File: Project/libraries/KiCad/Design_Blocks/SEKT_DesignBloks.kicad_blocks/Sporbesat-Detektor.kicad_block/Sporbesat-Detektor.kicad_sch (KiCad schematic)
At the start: 14 parts, among them J1 Screw_Terminal_01x02, J2 Screw_Terminal_01x02, J4 Conn_01x05_Socket, Q1 BC857, U1 PC847

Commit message: DCC signal
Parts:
- added R3: 2.2kΩ, PCM_JLCPCB:R_0805, symbol PCM_JLCPCB-Resistors:0805,1.8kΩ
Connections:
- net GNDDCC: now also R3.1
- net at C1.1, Q1.3 (C), R2.1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: now also R3.2
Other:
- moved on the sheet: C1, TP2

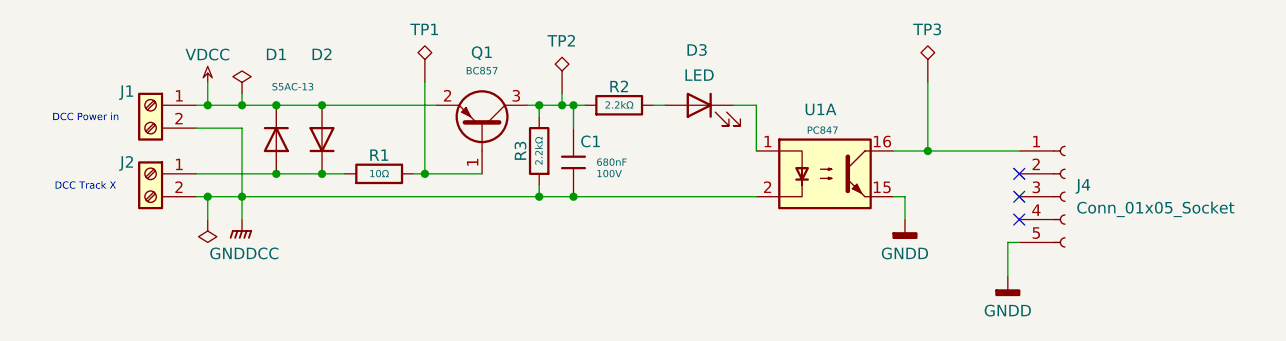
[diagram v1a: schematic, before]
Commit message: CanBus
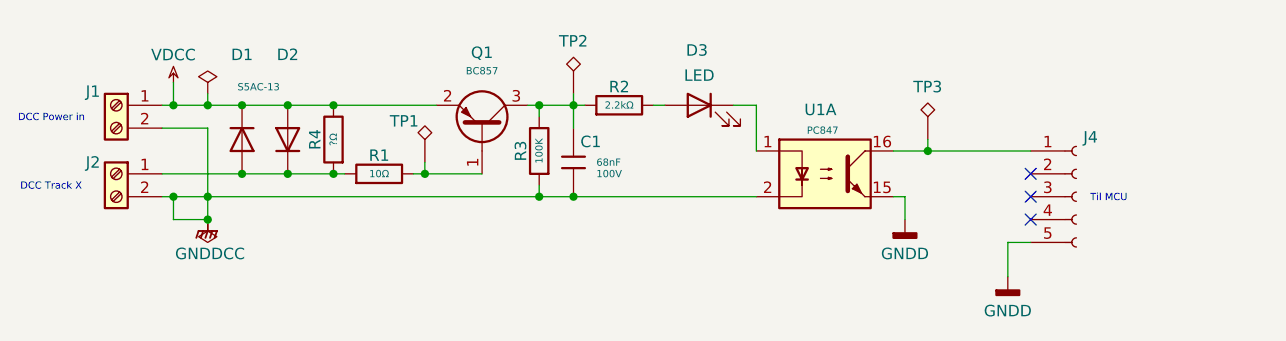
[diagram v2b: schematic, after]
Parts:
- added R4: ?Ω, PCM_JLCPCB:R_0805, symbol PCM_JLCPCB-Resistors:0805,1.8kΩ
- C1: value 680nF -> 68nF
- R3: value 2.2kΩ -> 100K
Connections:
- net VDCC: now also R4.2
- net at D1.2 (A), D2.1 (K), J2.1 (Pin_1)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: now also R4.1
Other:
- note added: "Til MCU"
- moved on the sheet: D1, D2, J1, J2, J4, TP1, TP2, TP3
